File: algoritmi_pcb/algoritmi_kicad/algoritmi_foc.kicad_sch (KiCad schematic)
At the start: 35 parts, among them IC1 MA710GQ-Z, IC2 AP2114HA-3.3TRG1, J2 53261-0371, J3 SMM-115-02-S-D-LC-K-TR, U1 TMC6300-LA-T

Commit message: my laptop version updated
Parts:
- added U2: MT6701CT-STD, Package_SO:SOIC-8_3.9x4.9mm_P1.27mm, symbol Memory_EEPROM:AT24CS64-SSHM

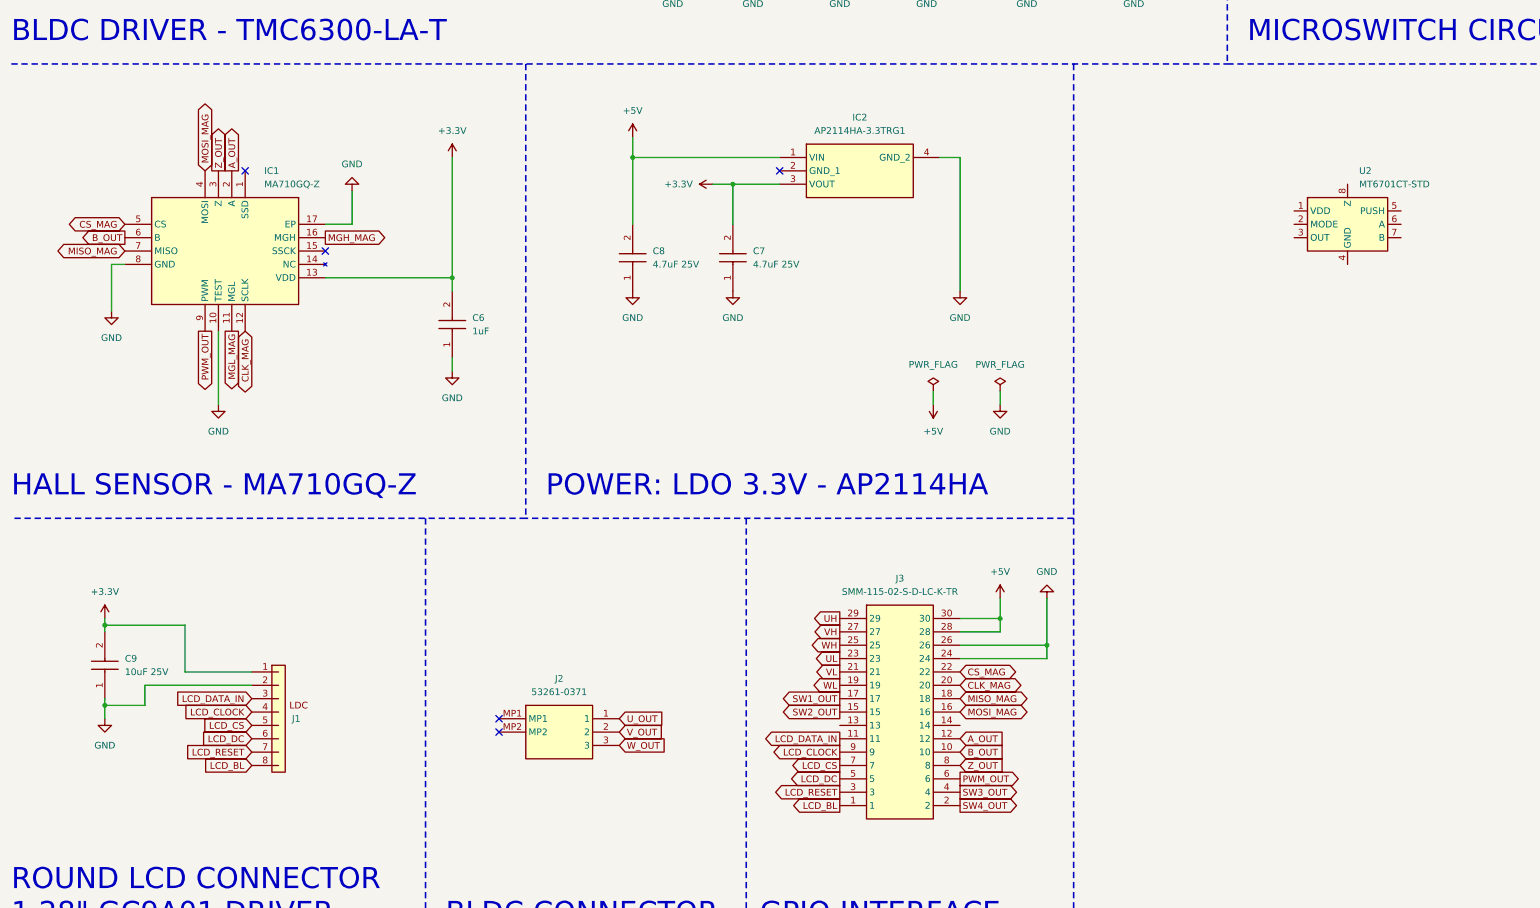
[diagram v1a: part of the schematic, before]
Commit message: finished version_1
doesn't have the presure sensitive part
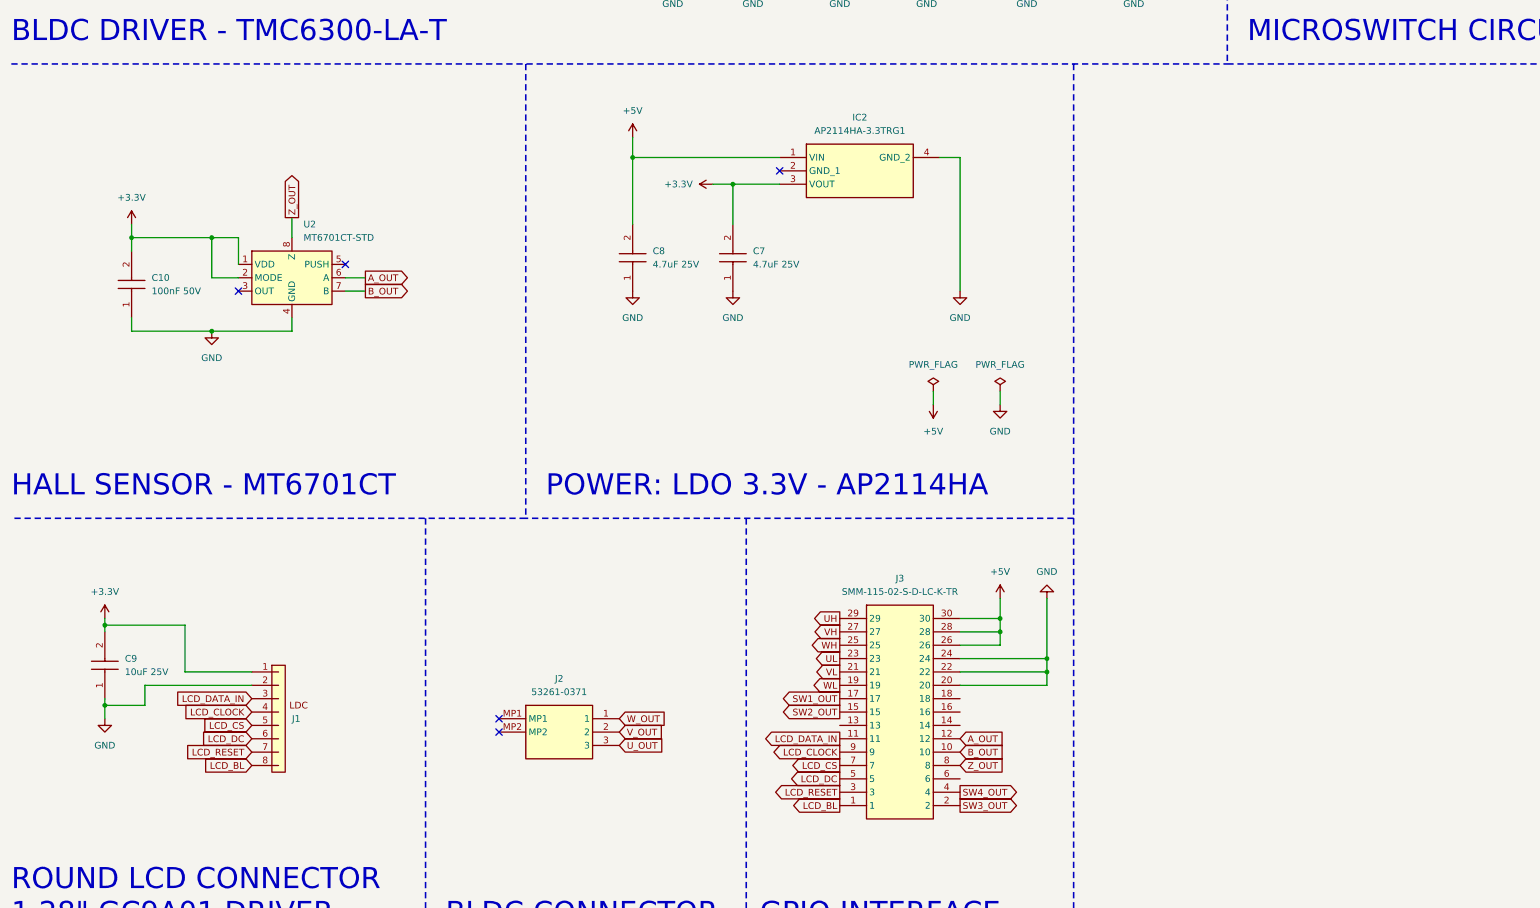
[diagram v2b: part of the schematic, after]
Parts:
- removed C6: 1uF, CAPC1608X90N, symbol SamacSys_Parts:CL10A105KA8NNNC
- removed IC1: MA710GQ-Z, QFN50P300X300X100-17N-D, symbol SamacSys_Parts:MA710GQ-Z
- added C10: 100nF 50V, CAPC1608X90N, symbol SamacSys_Parts:CL10B104KB8NNWC
- U2: value MT6701CT-STD -> MT6701CT-STD
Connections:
- net CLK_MAG is gone; now on net GND: J3.20
- net CS_MAG is gone; now on net GND: J3.22
- net +3.3V: now also U2.1 (VDD), U2.2 (MODE), C10.2
- net +5V: now also J3.26
- net A_OUT: now also U2.6 (A)
- net B_OUT: now also U2.7 (B)
- net GND: now also U2.4 (GND), C10.1; no longer J3.26
- net SW3_OUT: now also J3.2; no longer J3.4
- net SW4_OUT: now also J3.4; no longer J3.2
- net U_OUT: now also J2.3; no longer J2.1
- net W_OUT: now also J2.1; no longer J2.3
- net Z_OUT: now also U2.8 (Z)
- net MISO_MAG: no longer names the net of J3.18
- net MOSI_MAG: no longer names the net of J3.16
- net PWM_OUT: no longer names the net of J3.6
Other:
- note added: "HALL SENSOR - MT6701CT"
- note removed: "HALL SENSOR - MA710GQ-Z"
- moved on the sheet: U2

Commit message: New updates
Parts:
- J1: Mouser Part Number (none) -> 1; now not fitted
- MSW1, MSW2, MSW3, MSW4: Mouser Part Number (none) -> 906-XCF3Z1
- R3, R4: Mouser Part Number (none) -> 660-UR73VH2BTTDR150F
- U1: Manufacturer_Part_Number (none) -> TMC6300-LA-T; Mouser Part Number (none) -> 700-TMC6300-LA-T
- U2: LCSC Electronics Part Number (none) -> C2856764; Manufacturer_Part_Number (none) -> MT6701CT-STD
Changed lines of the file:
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@@
 			)
 		)
+		(property "Mouser Part Number" "906-XCF3Z1 "
+			(at 287.02 71.12 0)
+			(effects
+				(font
+					(size 1.27 1.27)
+				)
+				(hide yes)
+			)
+		)
 		(pin "1"
 		)
@@
 			)
 		)
+		(property "Mouser Part Number" "906-XCF3Z1 "
+			(at 287.02 55.88 0)
+			(effects
+				(font
+					(size 1.27 1.27)
+				)
+				(hide yes)
+			)
+		)
 		(pin "1"
 		)
@@
 			)
 		)
+		(property "LCSC Electronics Part Number" "C2856764"
+			(at 69.85 158.75 0)
+			(effects
+				(font
+					(size 1.27 1.27)
+				)
+				(hide yes)
+			)
+		)
+		(property "Manufacturer_Part_Number" "MT6701CT-STD"
+			(at 69.85 158.75 0)
+			(effects
+				(font
+					(size 1.27 1.27)
+				)
+				(hide yes)
+			)
+		)
 		(pin "8"
 		)
@@
 			)
 		)
-		(property "Mouser Part Number" ""
+		(property "Mouser Part Number" "660-UR73VH2BTTDR150F "
 			(at 119.38 576.2 0)
 			(effects
@@
 			)
 		)
+		(property "Manufacturer_Part_Number" "TMC6300-LA-T "
+			(at 88.9 30.48 0)
+			(effects
+				(font
+					(size 1.27 1.27)
+				)
+				(hide yes)
+			)
+		)
+		(property "Mouser Part Number" "700-TMC6300-LA-T "
+			(at 88.9 30.48 0)
+			(effects
+				(font
+					(size 1.27 1.27)
+				)
+				(hide yes)
+			)
+		)
 		(pin "20"
 		)
@@
 			)
 		)
+		(property "Mouser Part Number" "906-XCF3Z1 "
+			(at 287.02 86.36 0)
+			(effects
+				(font
+					(size 1.27 1.27)
+				)
+				(hide yes)
+			)
+		)
 		(pin "1"
 		)
@@
 			)
 		)
-		(property "Mouser Part Number" ""
+		(property "Mouser Part Number" "660-UR73VH2BTTDR150F "
 			(at 119.38 566.04 0)
 			(effects
@@
 			)
 		)
+		(property "Mouser Part Number" "906-XCF3Z1 "
+			(at 287.02 41.91 0)
+			(effects
+				(font
+					(size 1.27 1.27)
+				)
+				(hide yes)
+			)
+		)
 		(pin "1"
 		)
@@
 		(in_bom yes)
 		(on_board yes)
-		(dnp no)
+		(dnp yes)
 		(property "Reference" "J1"
 			(at 69.85 242.57 0)
@@
 			(at 53.34 254 0)
 			(effects
+				(font
+					(size 1.27 1.27)
+				)
+				(hide yes)
+			)
+		)
+		(property "Mouser Part Number" "1"
+			(at 53.34 254 0)
+			(effects

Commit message: updates
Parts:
- added C11, C13, C14, C15: 0.1uF, Capacitor_SMD:C_0603_1608Metric, symbol Device:C_Small
- added C12, C6: 10uF, Capacitor_SMD:C_0805_2012Metric, symbol Device:C_Small
- added J4: A, SolderPads:SolderPads_2mm_3_STRAIN, symbol Connector_Generic:Conn_01x03
- added J5: B, SolderPads:SolderPads_2mm_3_STRAIN, symbol Connector_Generic:Conn_01x03
- added L1: 3.3uH, Inductor_SMD:L_0805_2012Metric, symbol Device:L_Small
- added NT1: NetTie_2, NetTie:NetTie-2_SMD_Pad0.5mm, symbol Device:NetTie_2
- added Q1: MMBT4403, Package_TO_SOT_SMD:SOT-23, symbol Device:Q_PNP_BEC
- added R15, R16, R17, R18: 330, Resistor_SMD:R_2512_6332Metric, symbol Device:R_Small
- added R19, R20: 100, Resistor_SMD:R_0603_1608Metric, symbol Device:R_Small
- added R21: 10k, Resistor_SMD:R_0603_1608Metric, symbol Device:R_Small
- added R22: 8.2k, Resistor_SMD:R_0603_1608Metric, symbol Device:R_Small
- added U3: HX711, Package_SO:SOIC-16_3.9x9.9mm_P1.27mm, symbol strain:HX711
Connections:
- net GND: now also NT1.2
- new net: Q1.1 (B), U3.2 (BASE)
- new net: L1.1, Q1.3 (C), R21.1, U3.3 (AVDD)
- new net: R21.2, R22.1, U3.4 (VFB)
- new net: C14.1, R20.2, U3.8 (INA+)
- new net: C14.2, R19.1, U3.7 (INA-)
- new net: C15.2, U3.6 (VBG)
- new net +3V3: C12.1, C13.1, Q1.2 (E), U3.1 (VSUP), U3.15 (RATE), U3.16 (DVDD)
- new net GNDA: C11.2, C12.2, C13.2, C15.1, C6.2, J4.3 (Pin_3), J5.3 (Pin_3), NT1.1, R16.2, R18.1, R22.2, U3.10 (INB+), U3.14 (XI), U3.5 (AGND), U3.9 (INB-)
- new net STRAIN_DO: U3.12 (DOUT)
- new net STRAIN_E+: C11.1, C6.1, J4.1 (Pin_1), J5.1 (Pin_1), L1.2, R15.1, R17.2
- new net STRAIN_S+: J4.2 (Pin_2), R15.2, R16.1, R20.1
- new net STRAIN_S-: J5.2 (Pin_2), R17.1, R18.2, R19.2
- new net STRAIN_SCK: U3.11 (PD_SCK)
- no-connect marks 9 -> 10
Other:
- note added: "Rate=1 --> 80 samples per second"
- note added: "STRAIN SENSOR - HX711"

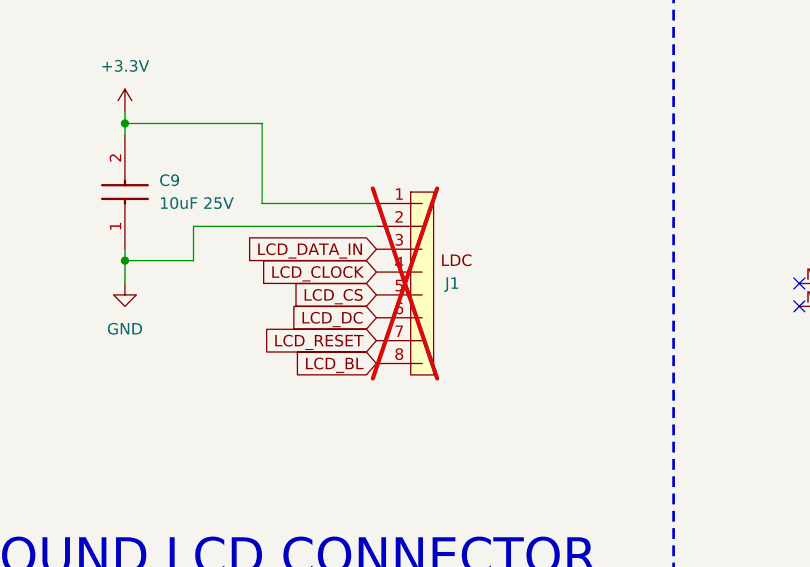
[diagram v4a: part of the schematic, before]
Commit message: adding the presure sensitive click pcb
I forgot to put it in the right position :)
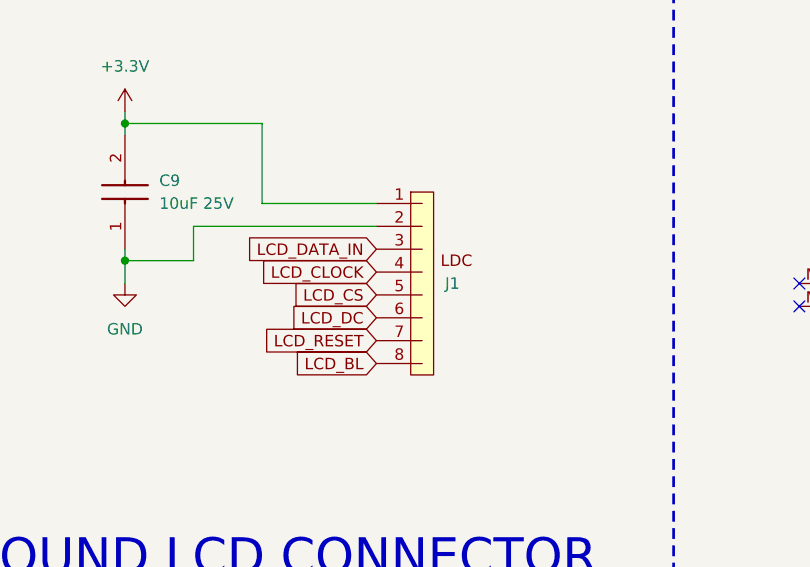
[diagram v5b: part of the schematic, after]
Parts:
- J1: now fitted
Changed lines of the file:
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@@
 		(in_bom yes)
 		(on_board yes)
-		(dnp yes)
+		(dnp no)
 		(property "Reference" "J1"
 			(at 69.85 242.57 0)
